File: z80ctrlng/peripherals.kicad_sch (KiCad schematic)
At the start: 33 parts, among them J10 SM04B-SRSS-TB, J11 USB_B_Micro, J3 UEXT, J4 UPDI, J5 XKTF-0803-0, J7 UXCS, J8 SERIAL, Q1 BSS138, Q2 BSS138, SW1 BUS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

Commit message: Final touches... I hope
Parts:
- removed J4: UPDI, Connector_PinHeader_2.54mm:PinHeader_1x04_P2.54mm_Horizontal, symbol Connector_Generic:Conn_01x04
- removed J8: SERIAL, Connector_PinHeader_2.54mm:PinHeader_1x04_P2.54mm_Horizontal, symbol Connector_Generic:Conn_01x04
- added C3: 0.1uf, Capacitor_SMD:C_0402_1005Metric, symbol Device:C_Small
- added D2, D3: 1N5819WS, Diode_SMD:D_SOD-323_HandSoldering, symbol Device:D_Small
- added J4: DEBUG, Connector_PinHeader_2.54mm:PinHeader_2x04_P2.54mm_Horizontal, symbol Connector_Generic:Conn_02x04_Odd_Even
- added R2: 1K, Resistor_SMD:R_0402_1005Metric, symbol Device:R_Small
- J11: value USB_B_Micro -> U254-051T-4BH81-S2S; footprint Connector_USB:USB_Micro-B_XKB_U254-051T-4BH83-F1S -> SamacSys_Parts:U254051T4BH81S2S
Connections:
- net +3.3V: now also R11.1, R12.1, R13.1, D3.2 (A); no longer BT1.1 (+), C3.1, U3.8 (VDD)
- net +5V: now also U7.16 (VCC), C3.1, J4.3 (Pin_3), J4.4 (Pin_4)
- net GND: now also J11.5 (GND), U7.1 (GND), C3.2, J4.5 (Pin_5), J4.6 (Pin_6); no longer J5.MP1, J5.MP2, J5.MP3, J5.MP4
- net UPDI: now also J4.7 (Pin_7)
- net ~{RESET}: now also J4.1 (Pin_1)
- net TXU: now reaches U7.2 (TXD)
- net RXU: now reaches U7.3 (RXD)
- net at U7.5 (UD+): now also J11.2 (D-)
- net at U7.6 (UD-): now also J11.3 (D+)
- net CTS: now reaches U7.9 (~{CTS})
- net RX3 renamed RX3V
- net TX3 renamed TX3V
- net ~{SDCS} renamed ~{SS}
- new net: C3.1, D2.1 (K), D3.1 (K), U3.8 (VDD)
- new net: D2.2 (A), R2.1
- new net: BT1.1 (+), R2.2
- new net RXB: J4.8 (Pin_8)
- new net TXB: J4.2 (Pin_2)
- no-connect marks 5 -> 20
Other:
- moved on the sheet: BT1, C3, C6, C9, D1, R10, R11, R12, U7

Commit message: Fixing mistakes on RX/TX, better isolation for RTC
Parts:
- removed C2: 0.6pf, Capacitor_SMD:C_0402_1005Metric, symbol Device:C_Small
- removed C6: 0.1uf, Capacitor_SMD:C_0402_1005Metric, symbol Device:C_Small
- removed J4: DEBUG, Connector_PinHeader_2.54mm:PinHeader_2x04_P2.54mm_Horizontal, symbol Connector_Generic:Conn_02x04_Odd_Even
- removed R2: 10K, Resistor_SMD:R_0402_1005Metric, symbol Device:R
- removed SW1: RESET, Button_Switch_THT:SW_Tactile_SPST_Angled_PTS645Vx31-2LFS, symbol Switch:SW_Push
- added NT1: NetTie_2, NetTie:NetTie-2_SMD_Pad0.5mm, symbol Device:NetTie_2
- C1: value 0.6pf -> 27pf; footprint Capacitor_SMD:C_0402_1005Metric -> Capacitor_SMD:C_0603_1608Metric
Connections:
- net GND: now also J5.G1 (DET), NT1.2; no longer C1.2
- net RXU: now also U7.2 (TXD); no longer U7.3 (RXD)
- net TXU: now also U7.3 (RXD); no longer U7.2 (TXD)
- net at U3.1 (OSCI), Y1.2: now also C1.2; no longer C1.1
- new net GND1: C1.1, NT1.1
- no-connect marks 20 -> 21
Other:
- moved on the sheet: BT1, C1, C3, C9, D2, D3, J10, J11, J3, J7, R2, U7

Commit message: More final touches o.O
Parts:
- removed J7: UXCS, Connector_PinHeader_2.54mm:PinHeader_2x04_P2.54mm_Vertical, symbol Connector_Generic:Conn_02x04_Odd_Even
- removed R2: 1K, Resistor_SMD:R_0402_1005Metric, symbol Device:R_Small
- added JP1: AUTORESET, Jumper:SolderJumper-2_P1.3mm_Bridged_Pad1.0x1.5mm, symbol Jumper:Jumper_2_Bridged
- added Q1: BSS138, Package_TO_SOT_SMD:SOT-23, symbol Transistor_FET:BSS138
- R10: value 100 -> 1K
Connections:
- net +3.3V: now also J5.P4 (VDD), Q1.1 (G); no longer J5.P5 (CLK)
- net GND: now also J5.MP1, J5.MP2, J5.MP3, J5.MP4, J5.P6 (VSS); no longer J5.P7 (DAT0)
- net MISO: now also J5.P7 (DAT0); no longer J5.P8 (DAT1)
- net MOSI: now also J5.P3 (CMD); no longer J5.P4 (VDD)
- net SCK: now also J5.P5 (CLK); no longer J5.P6 (VSS)
- net ~{RESET}: now also JP1.2 (B); no longer C9.2
- net ~{SS}: now also J3.10 (Pin_10); no longer J5.P3 (CMD), R10.1, R12.2
- net at D2.2 (A): now also BT1.1 (+)
- net at J5.P2 (DAT3/CD): now also R10.1, R12.2, Q1.3 (D)
- net CTS: no longer names the net of U7.9 (~{CTS})
- new net: C9.2, JP1.1 (A)
- new net ~{SDCS}: Q1.2 (S)
- no-connect marks 21 -> 18
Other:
- moved on the sheet: BT1, C10, D1, J5, R10, R11, R12, R13, R14

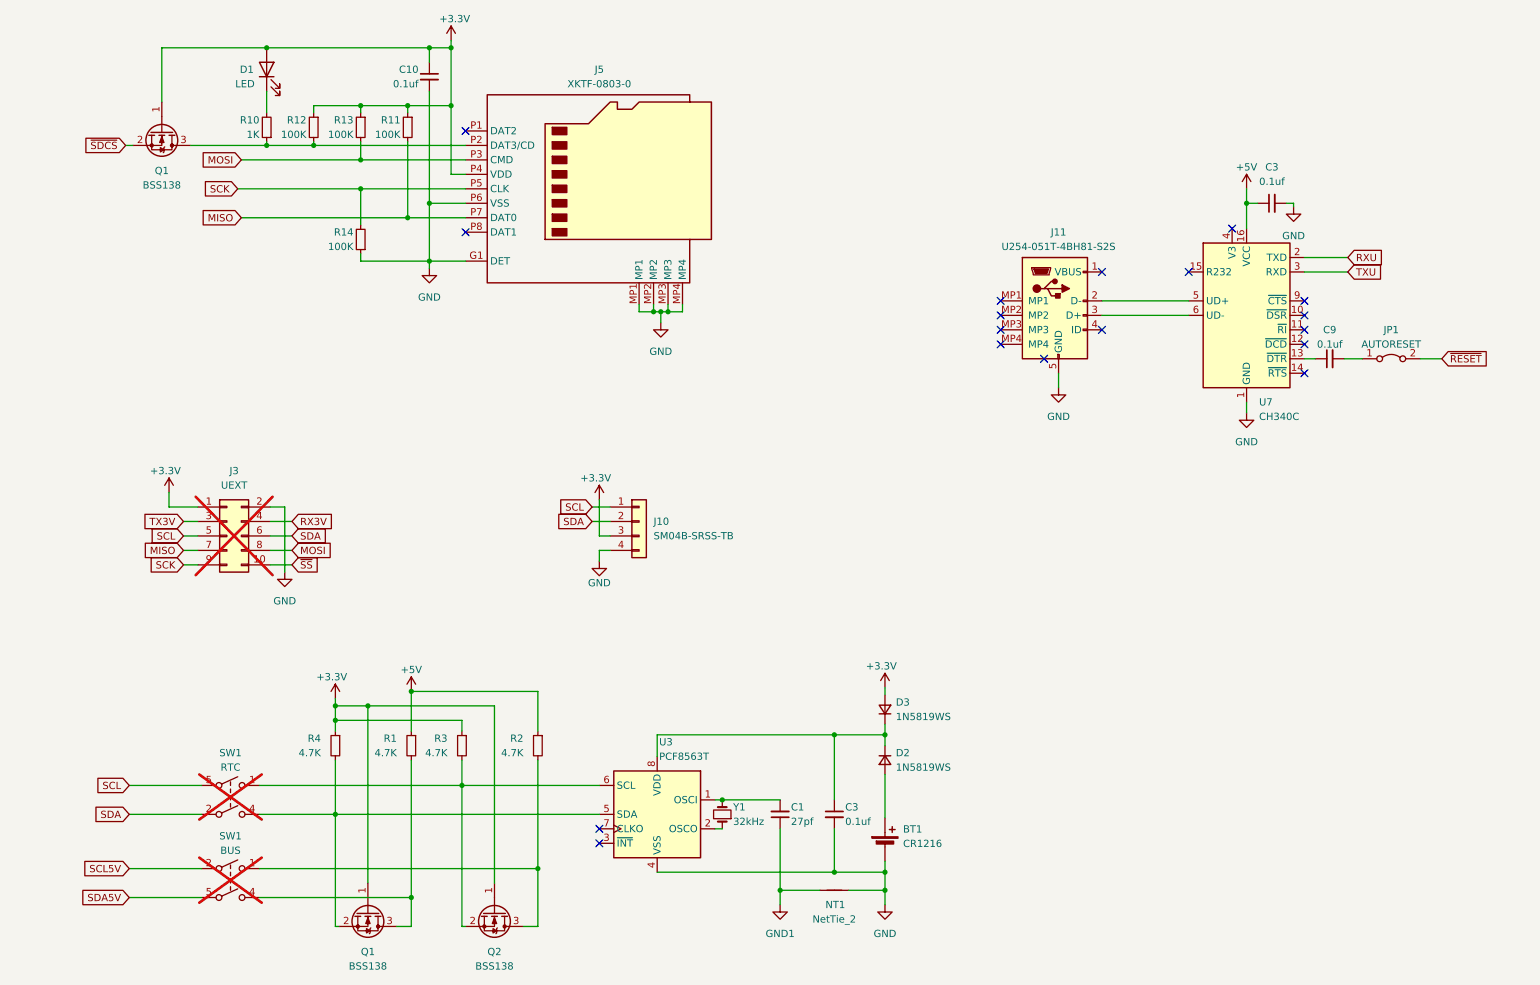
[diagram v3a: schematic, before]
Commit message: Muntz unnecessary jumpers/switches; add SerialUDPI programmer; cleanup layout
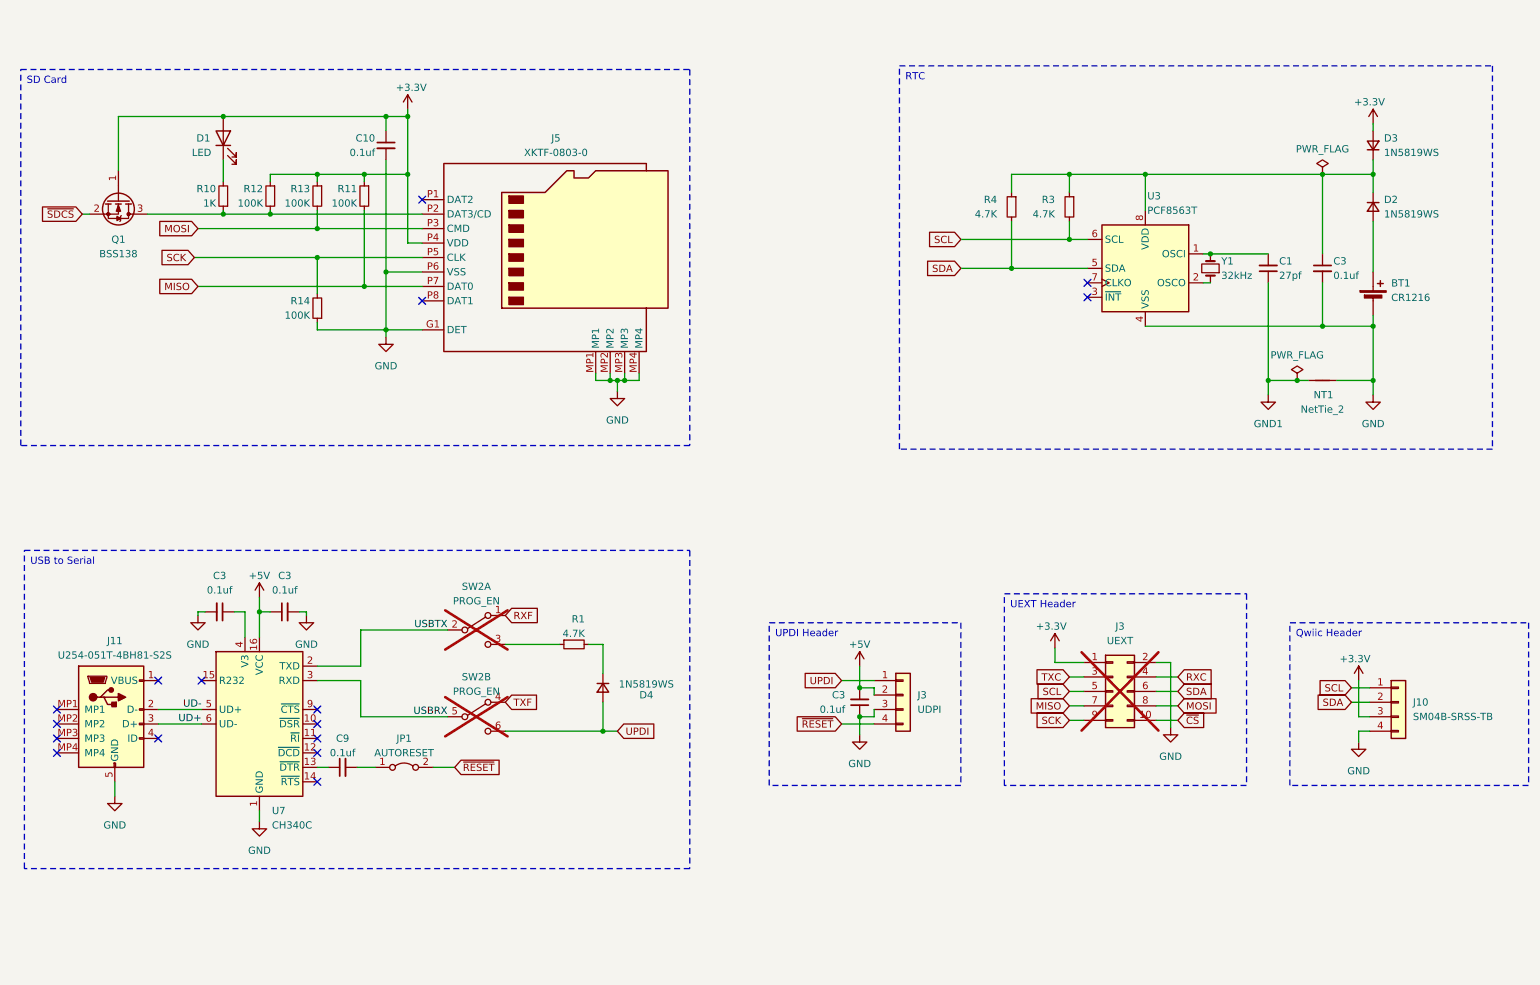
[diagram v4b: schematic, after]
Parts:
- removed Q1, Q2: BSS138, Package_TO_SOT_SMD:SOT-23, symbol Transistor_FET:BSS138
- removed R2: 4.7K, Resistor_SMD:R_0402_1005Metric, symbol Device:R_Small
- removed SW1: BUS, SamacSys_Parts:JS202011CQN, symbol Switch:SW_DPST
- removed SW1: RTC, SamacSys_Parts:JS202011CQN, symbol Switch:SW_DPST
- added C3 (x2): 0.1uf, Capacitor_SMD:C_0402_1005Metric, symbol Device:C_Small
- added D4: 1N5819WS, Diode_SMD:D_SOD-323_HandSoldering, symbol Device:D_Small
- added J3: UDPI, Connector_PinHeader_2.54mm:PinHeader_1x04_P2.54mm_Horizontal, symbol Connector_Generic:Conn_01x04
- added SW2: PROG_EN, SamacSys_Parts:JS202011CQN, symbol Switch:SW_DPDT_x2
- JP1: footprint Jumper:SolderJumper-2_P1.3mm_Bridged_Pad1.0x1.5mm -> Jumper:SolderJumper-2_P1.3mm_Bridged_RoundedPad1.0x1.5mm
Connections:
- net +3.3V: no longer R3.1, R4.1
- net +5V: now also C3.2, J3.2 (Pin_2); no longer R1.1
- net GND: now also C3.1, C3.2, J3.3 (Pin_3)
- net SCL: now also R3.2, U3.6 (SCL)
- net SDA: now also R4.2, U3.5 (SDA)
- net ~{RESET}: now also J3.4 (Pin_4)
- net at R1.2: now also D4.1 (K)
- net at U7.4 (V3): now also C3.1
- net UD-: now reaches J11.2 (D-), U7.5 (UD+)
- net UD+: now reaches J11.3 (D+), U7.6 (UD-)
- net at C3.1, D2.1 (K), D3.1 (K)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: now also R3.1, R4.1
- net RX3V renamed RXC
- net RXU renamed USBTX
- net USBTX: now also SW2.2 (B)
- net TX3V renamed TXC
- net TXU renamed USBRX
- net USBRX: now also SW2.5 (B)
- net ~{SS} renamed ~{CS}
- new net: R1.1, SW2.3 (C)
- new net RXF: SW2.1 (A)
- new net TXF: SW2.4 (A)
- new net UPDI: D4.2 (A), J3.1 (Pin_1), SW2.6 (C)
- no-connect marks 18 -> 16
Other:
- moved on the sheet: BT1, C1, C10, C3, C9, D1, D2, D3, J10, J11, J3, J5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

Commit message: Rearrange to make fast 3.3V buses shorter
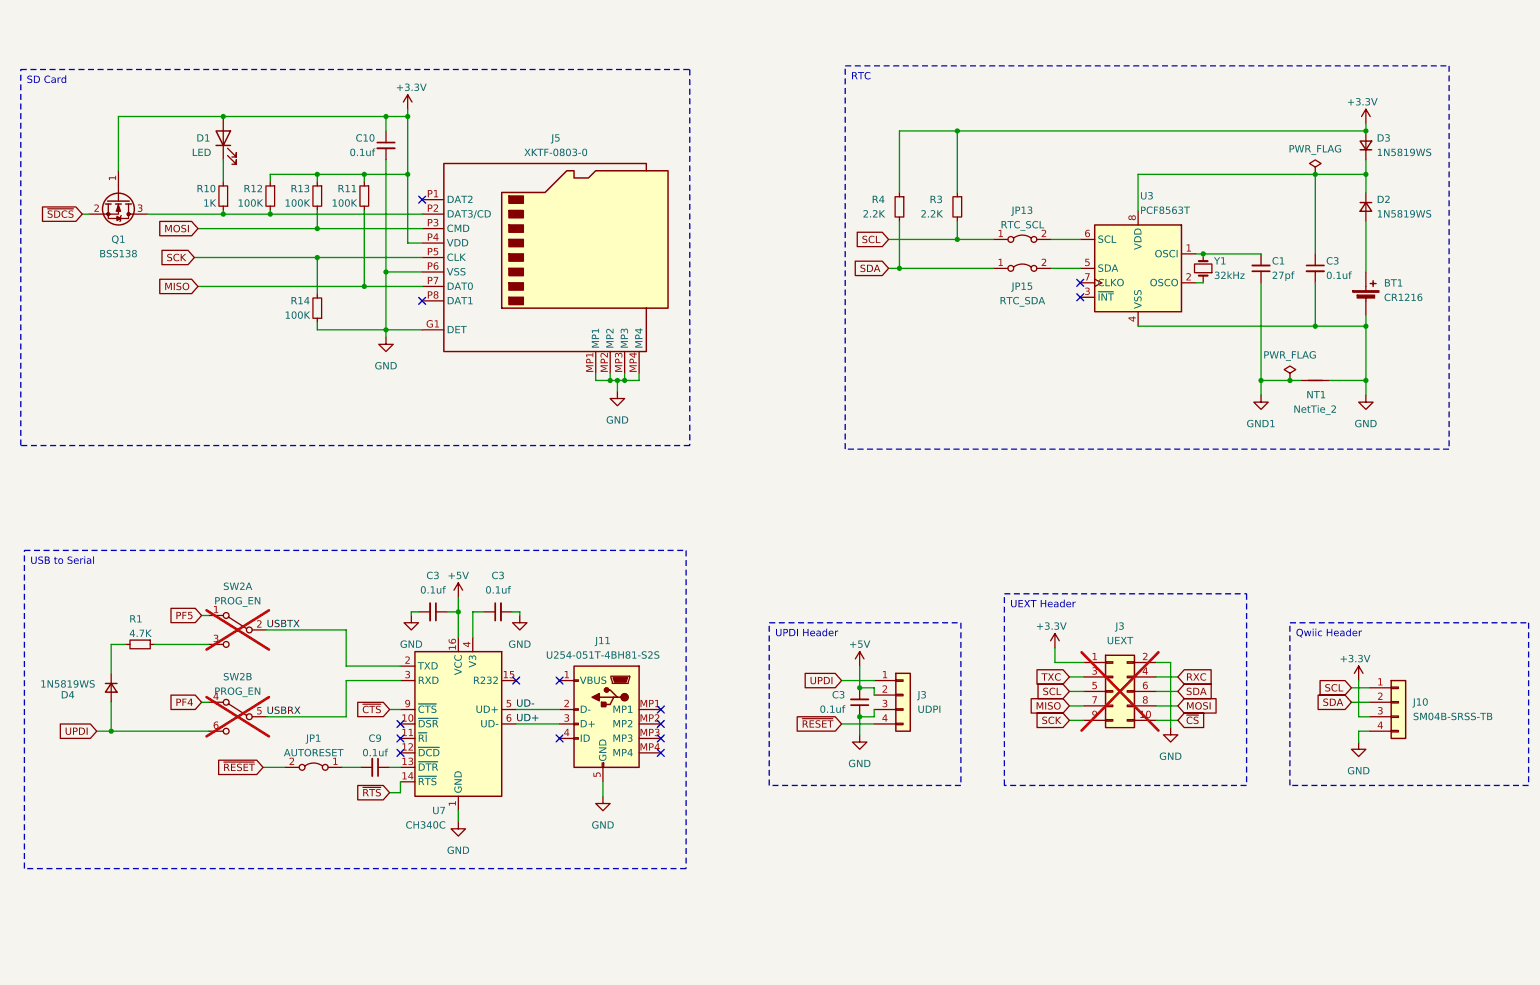
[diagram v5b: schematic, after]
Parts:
- added JP13: RTC_SCL, Jumper:SolderJumper-2_P1.3mm_Bridged_RoundedPad1.0x1.5mm, symbol Jumper:Jumper_2_Bridged
- added JP15: RTC_SDA, Jumper:SolderJumper-2_P1.3mm_Bridged_RoundedPad1.0x1.5mm, symbol Jumper:Jumper_2_Bridged
- C1: footprint Capacitor_SMD:C_0603_1608Metric -> Capacitor_SMD:C_0603_1608Metric_Pad1.08x0.95mm_HandSolder
- R3, R4: value 4.7K -> 2.2K
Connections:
- net +3.3V: now also R3.1, R4.1
- net SCL: now also JP13.1 (A); no longer U3.6 (SCL)
- net SDA: now also JP15.1 (A); no longer U3.5 (SDA)
- net ~{RTS}: now reaches U7.14 (~{RTS})
- net ~{CTS}: now reaches U7.9 (~{CTS})
- net at C3.1, D2.1 (K), D3.1 (K)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: no longer R3.1, R4.1
- net RXF renamed PF5
- net TXF renamed PF4
- new net: JP15.2 (B), U3.5 (SDA)
- new net: JP13.2 (B), U3.6 (SCL)
- no-connect marks 16 -> 14
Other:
- moved on the sheet: BT1, C1, C3, C9, D2, D3, D4, J11, JP1, NT1, R1, R3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

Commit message: Updating silkscreen
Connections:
- net PF4 renamed TXF
- net PF5 renamed RXF
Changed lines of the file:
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@@
     )
   )
-  (global_label "PF5" (shape input) (at 46.355 120.015 180) (fields_autoplaced)
+  (global_label "RXF" (shape input) (at 46.355 120.015 180) (fields_autoplaced)
     (effects (font (size 1.27 1.27)) (justify right))
     (property "Intersheetrefs" "${INTERSHEET_REFS}" (at 39.8017 120.015 0)
@@
     )
   )
-  (global_label "PF4" (shape input) (at 46.355 135.255 180) (fields_autoplaced)
+  (global_label "TXF" (shape input) (at 46.355 135.255 180) (fields_autoplaced)
     (effects (font (size 1.27 1.27)) (justify right))
-    (property "Intersheetrefs" "${INTERSHEET_REFS}" (at 39.8017 135.255 0)
+    (property "Intersheetrefs" "${INTERSHEET_REFS}" (at 40.1041 135.255 0)
       (effects (font (size 1.27 1.27)) (justify right) hide)
     )

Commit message: Misc tweaks to boards
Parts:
- J3: now not fitted
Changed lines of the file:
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@@
   )
   (symbol (lib_id "Connector_Generic:Conn_01x04") (at 169.545 133.985 0) (unit 1)
-    (in_bom yes) (on_board yes) (dnp no) (fields_autoplaced)
+    (in_bom yes) (on_board yes) (dnp yes) (fields_autoplaced)
     (property "Reference" "J3" (at 172.085 133.985 0)
       (effects (font (size 1.27 1.27)) (justify left))

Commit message: Put resistor before switch to avoid parasitic powering of the board
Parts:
- R1: value 4.7K -> 1K
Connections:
- net USBTX: now also R1.2; no longer U7.2 (TXD)
- net at R1.1: now also U7.2 (TXD); no longer SW2.3 (C)
- net at D4.1 (K): now also SW2.3 (C); no longer R1.2
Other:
- moved on the sheet: R1
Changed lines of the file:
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@@
-    (stroke (width 0) (type default))
-  )
-  (wire (pts (xy 33.02 125.095) (xy 30.48 125.095))
     (stroke (width 0) (type default))
   )
@@
     (stroke (width 0) (type default))
   )
-  (wire (pts (xy 71.755 122.555) (xy 57.785 122.555))
+  (wire (pts (xy 71.755 122.555) (xy 70.485 122.555))
     (stroke (width 0) (type default))
   )
@@
     (stroke (width 0) (type default))
   )
-  (wire (pts (xy 47.625 125.095) (xy 38.1 125.095))
+  (wire (pts (xy 30.48 125.095) (xy 47.625 125.095))
     (stroke (width 0) (type default))
   )
@@
   )
   (wire (pts (xy 58.42 42.545) (xy 58.42 43.815))
+    (stroke (width 0) (type default))
+  )
+  (wire (pts (xy 65.405 122.555) (xy 57.785 122.555))
     (stroke (width 0) (type default))
   )
@@
     )
   )
-  (symbol (lib_id "Device:R_Small") (at 35.56 125.095 270) (unit 1)
+  (symbol (lib_id "Device:R_Small") (at 67.945 122.555 270) (unit 1)
     (in_bom yes) (on_board yes) (dnp no)
-    (property "Reference" "R1" (at 33.655 120.65 90)
-      (effects (font (size 1.27 1.27)) (justify left))
-    )
-    (property "Value" "4.7K" (at 33.655 123.19 90)
-      (effects (font (size 1.27 1.27)) (justify left))
-    )
-    (property "Footprint" "Resistor_SMD:R_0402_1005Metric" (at 35.56 125.095 0)
-      (effects (font (size 1.27 1.27)) hide)
-    )
-    (property "Datasheet" "~" (at 35.56 125.095 0)
-      (effects (font (size 1.27 1.27)) hide)
-    )
+    (property "Reference" "R1" (at 66.04 118.11 90)
+      (effects (font (size 1.27 1.27)) (justify left))
+    )
+    (property "Value" "1K" (at 66.04 120.65 90)
+      (effects (font (size 1.27 1.27)) (justify left))
+    )
+    (property "Footprint" "Resistor_SMD:R_0402_1005Metric" (at 67.945 122.555 0)
+      (effects (font (size 1.27 1.27)) hide)
+    )
+    (property "Datasheet" "~" (at 67.945 122.555 0)
+      (effects (font (size 1.27 1.27)) hide)
+    )
